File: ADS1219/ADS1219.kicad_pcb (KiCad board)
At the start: 2 copper layers, 25 x 25 mm, 24 parts, among them J1 Conn_01x04, J2 Conn_01x06, J3 Conn_01x04, SW1 CUS-14B_NDC, SW2 CUS-14B_NDC, U1 ADS1219IPW

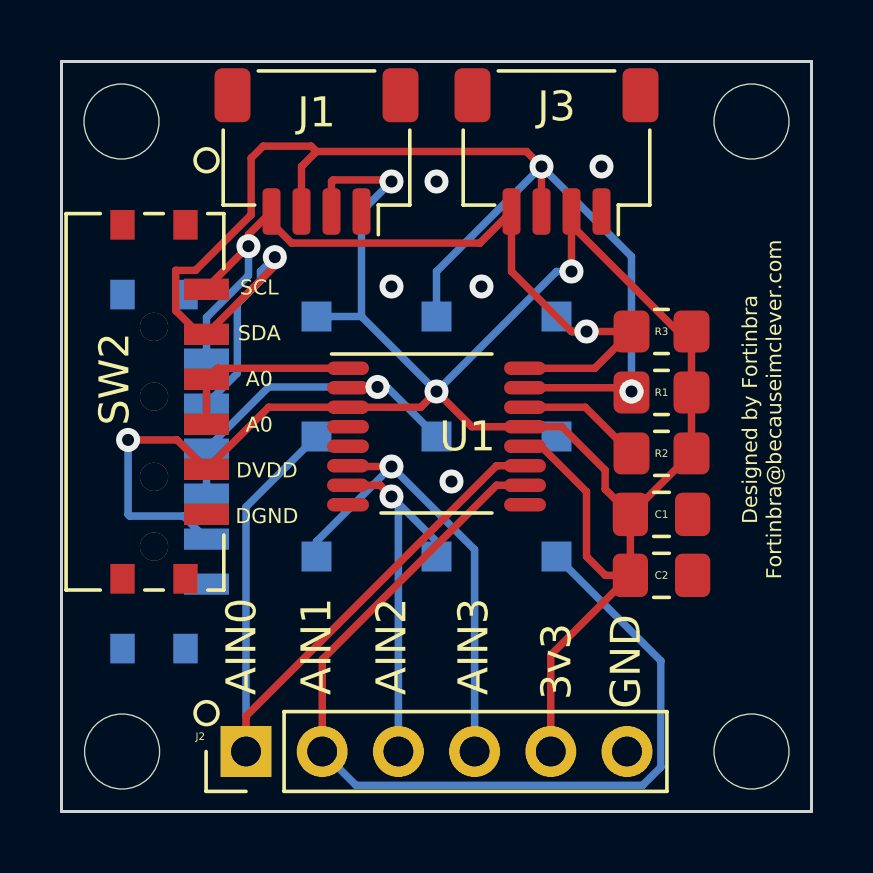
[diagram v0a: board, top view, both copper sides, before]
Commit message: Revert "Adding slider for address programming"
This reverts commit 487b6004aa2a68d069b1c4fba08261144dd1fb57.
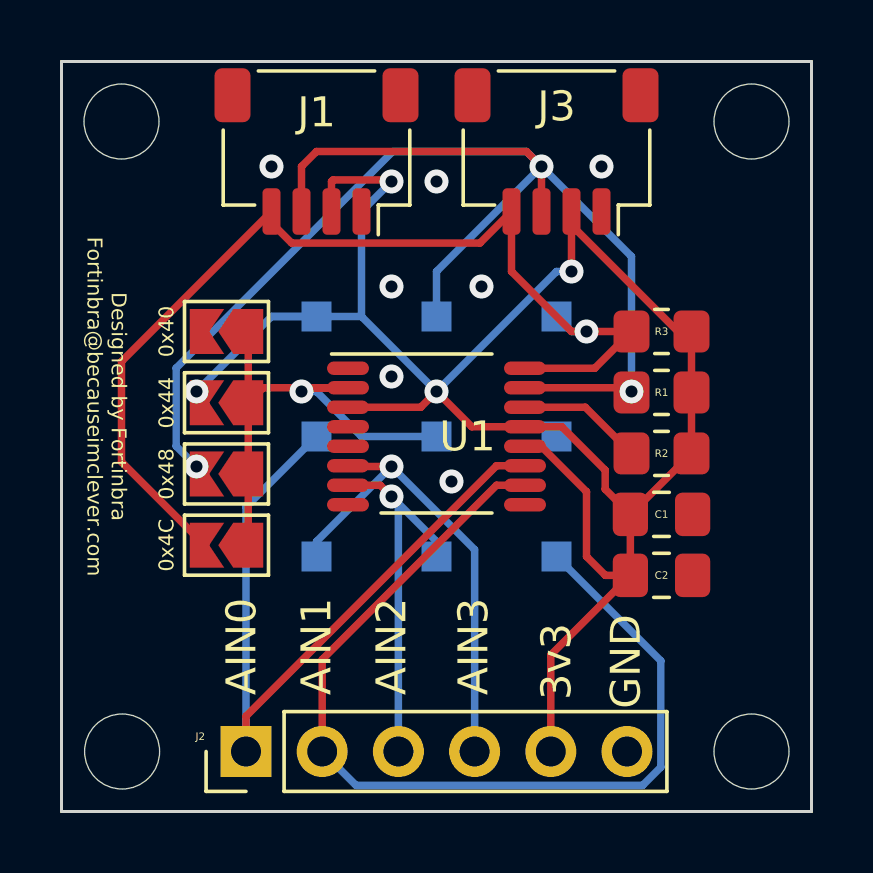
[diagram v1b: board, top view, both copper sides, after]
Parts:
- removed SW1, SW2: CUS-14B_NDC, ul_CUS-14TB:CUS-14TB
- added JP1: SolderJumper_2_Open, Jumper:SolderJumper-2_P1.3mm_Open_TrianglePad1.0x1.5mm, F.Cu at (163.5, 83.0)
- added JP2: SolderJumper_2_Open, Jumper:SolderJumper-2_P1.3mm_Open_TrianglePad1.0x1.5mm, F.Cu at (163.5, 85.4)
- added JP3: SolderJumper_2_Open, Jumper:SolderJumper-2_P1.3mm_Open_TrianglePad1.0x1.5mm, F.Cu at (163.5, 87.7)
- added JP4: SolderJumper_2_Open, Jumper:SolderJumper-2_P1.3mm_Open_TrianglePad1.0x1.5mm, F.Cu at (163.5, 90.1)
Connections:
- U1 pad 1: /A0 -> GND
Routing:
- net +3.3V: track 75.3 -> 67.8 mm
- net /SCL: track 29.0 -> 35.5 mm, vias 2 -> 1
- net /A0: track 6.37 -> 0.00 mm
- net /A1: track 11.7 -> 17.4 mm
- net GND: vias 5 -> 7
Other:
- board text removed: "A0"
- board text removed: "A1"
- board text removed: "DGND"
- board text removed: "DVDD"
- board text removed: "SCL"
- board text removed: "SDA"

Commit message: Adding slider for address programming
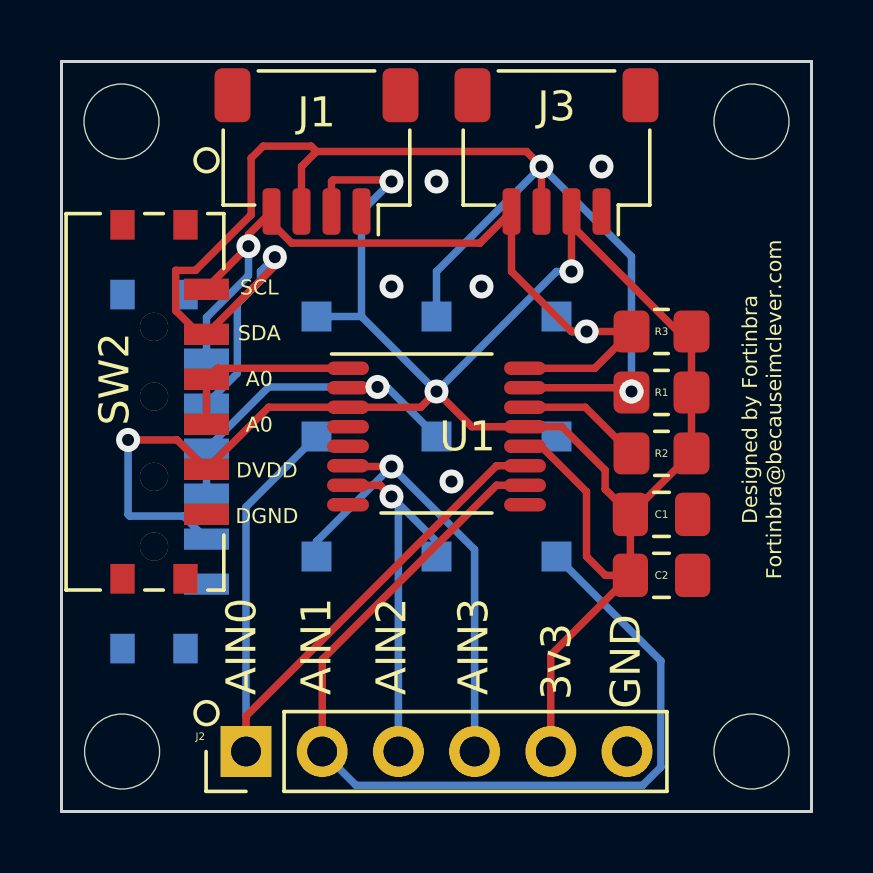
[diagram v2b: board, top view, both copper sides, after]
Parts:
- removed JP1, JP2, JP3, JP4: SolderJumper_2_Open, Jumper:SolderJumper-2_P1.3mm_Open_TrianglePad1.0x1.5mm
- added SW1: CUS-14B_NDC, ul_CUS-14TB:CUS-14TB, B.Cu at (160.8, 87.7)
- added SW2: CUS-14B_NDC, ul_CUS-14TB:CUS-14TB, F.Cu at (160.8, 85.3)
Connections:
- U1 pad 1: GND -> /A0
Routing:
- net +3.3V: track 67.8 -> 75.3 mm
- net /SCL: track 35.5 -> 29.0 mm, vias 1 -> 2
- net /A0: track 0.00 -> 6.37 mm
- net /A1: track 17.4 -> 11.7 mm
- net GND: vias 7 -> 5
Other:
- board text added: "A0"
- board text added: "A1"
- board text added: "DGND"
- board text added: "DVDD"
- board text added: "SCL"
- board text added: "SDA"
